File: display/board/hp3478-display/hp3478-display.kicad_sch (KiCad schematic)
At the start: 55 parts, among them J1 SFV10R-1ST, J2 DNP, U1 FT60F1x2, U2 SM16206

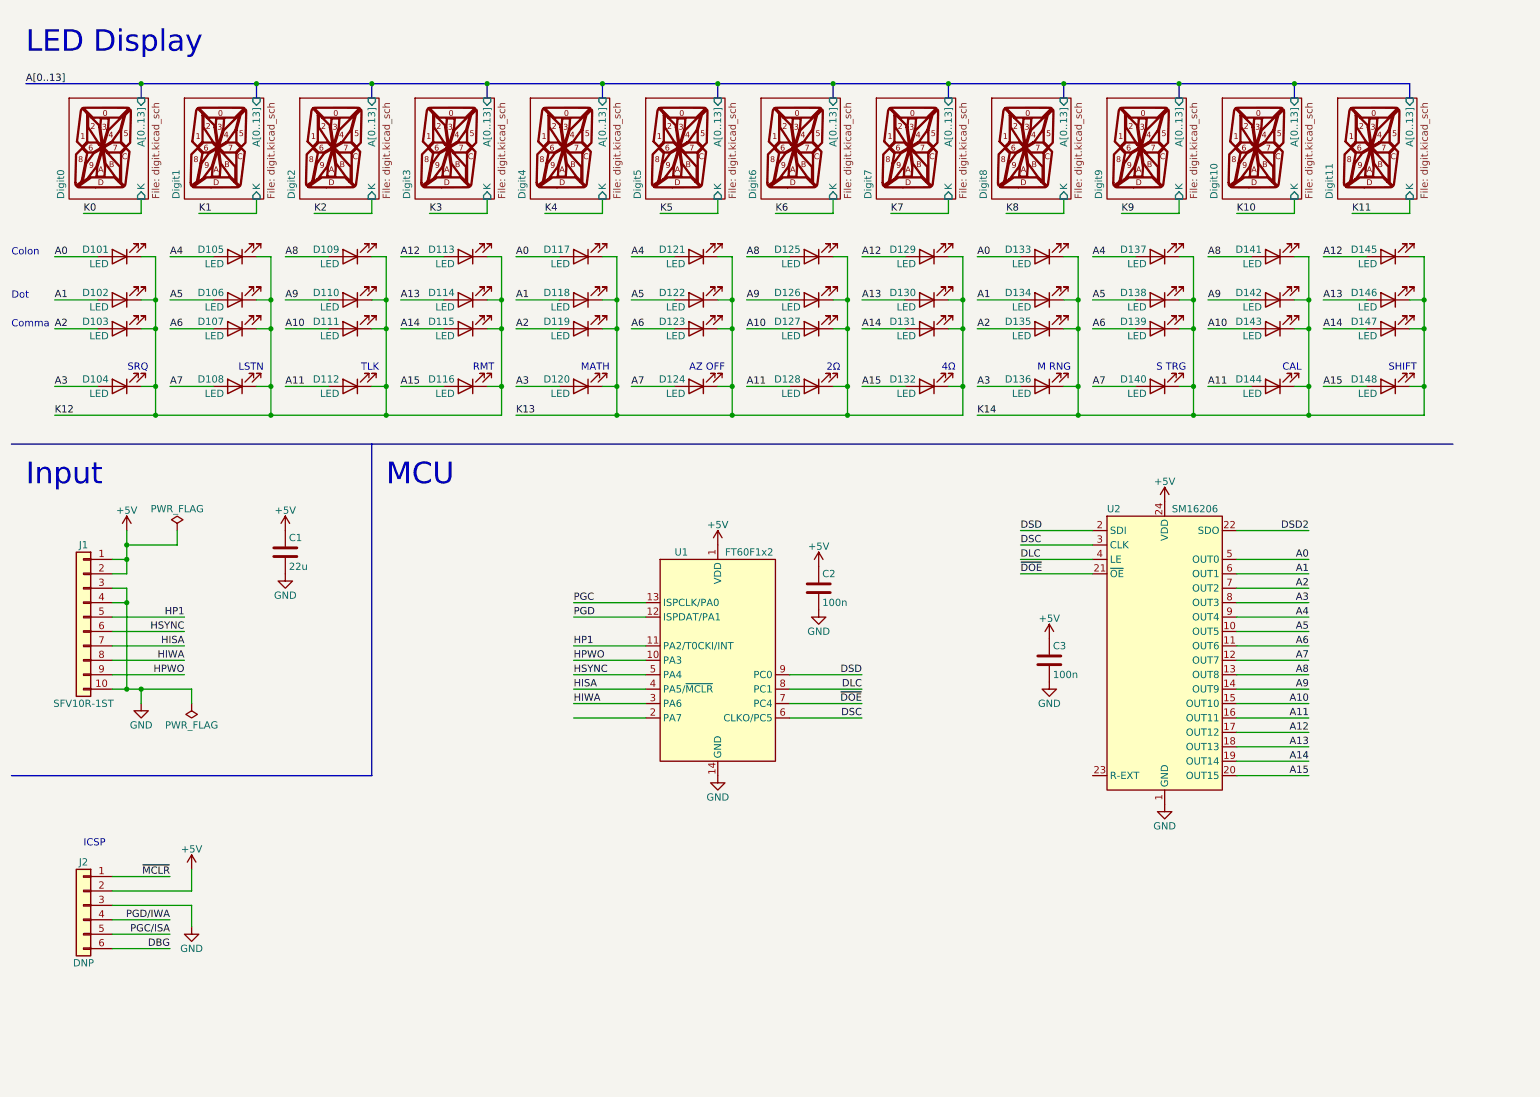
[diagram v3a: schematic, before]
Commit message: Improve workflow for getting digit shapes into KiCAD.
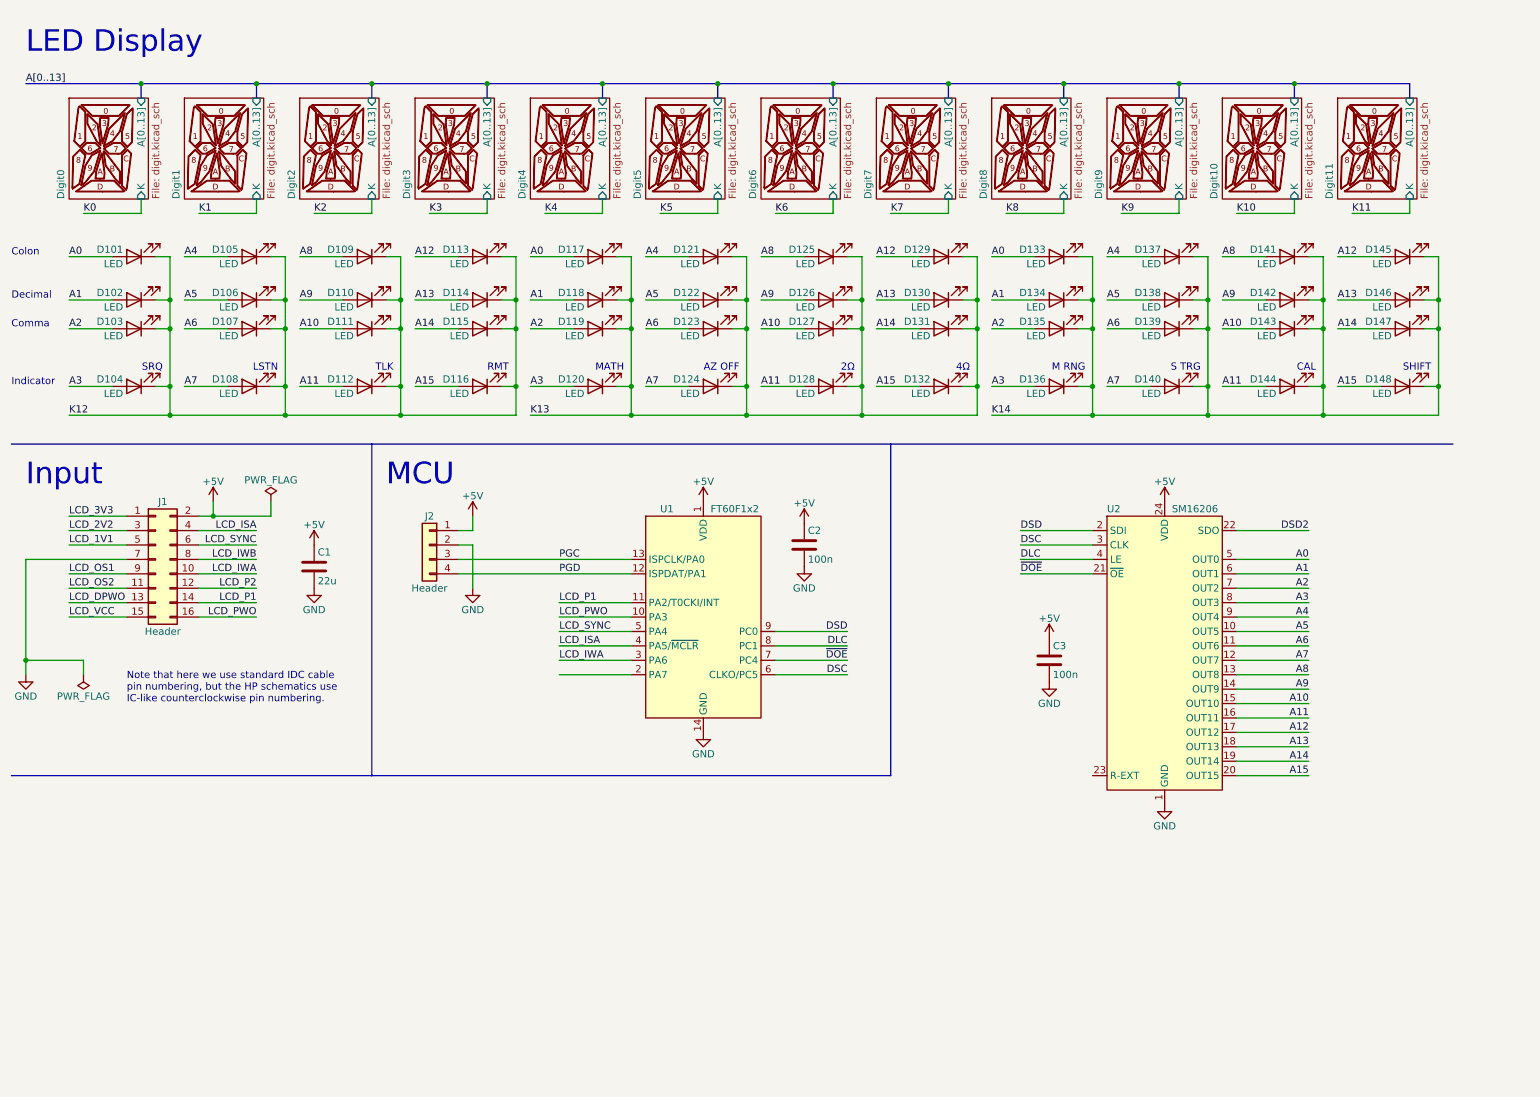
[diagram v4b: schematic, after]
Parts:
- removed J1: SFV10R-1ST, 0Local:Amphenol_SFV10R-1ST, symbol Connector_Generic:Conn_01x10
- removed J2: DNP, Connector_PinHeader_2.54mm:PinHeader_1x06_P2.54mm_Vertical, symbol Connector_Generic:Conn_01x06
- added J1: Header, Connector_PinHeader_2.54mm:PinHeader_2x08_P2.54mm_Vertical_SMD, symbol Connector_Generic:Conn_02x08_Odd_Even
- added J2: Header, Connector_PinHeader_2.54mm:PinHeader_1x04_P2.54mm_Vertical_SMD_Pin1Left, symbol Connector_Generic:Conn_01x04
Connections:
- net +5V: now also J1.2 (Pin_2), J2.1 (Pin_1)
- net GND: now also J1.7 (Pin_7), J2.2 (Pin_2)
- net PGC: now also J2.3 (Pin_3)
- net PGD: now also J2.4 (Pin_4)
- net HISA renamed LCD_ISA
- net LCD_ISA: now also J1.4 (Pin_4)
- net HIWA renamed LCD_IWA
- net LCD_IWA: now also J1.10 (Pin_10)
- net HP1 renamed LCD_P1
- net LCD_P1: now also J1.14 (Pin_14)
- net HPWO renamed LCD_PWO
- net LCD_PWO: now also J1.16 (Pin_16)
- net HSYNC renamed LCD_SYNC
- net LCD_SYNC: now also J1.6 (Pin_6)
- new net LCD_1V1: J1.5 (Pin_5)
- new net LCD_2V2: J1.3 (Pin_3)
- new net LCD_3V3: J1.1 (Pin_1)
- new net LCD_DPWO: J1.13 (Pin_13)
- new net LCD_IWB: J1.8 (Pin_8)
- new net LCD_OS1: J1.9 (Pin_9)
- new net LCD_OS2: J1.11 (Pin_11)
- new net LCD_P2: J1.12 (Pin_12)
- new net LCD_VCC: J1.15 (Pin_15)
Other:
- note added: "Decimal"
- note added: "Indicator"
- note added: "Note that here we use standard IDC cable pin numbering, but the HP schematics use IC-like counterclockwise pin numbering."
- note removed: "Dot"
- note removed: "ICSP"
- moved on the sheet: C1, C2, D101, D102, D103, D104, D105, D106, D107, D108, D109, D110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

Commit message: Add cathode drivers.
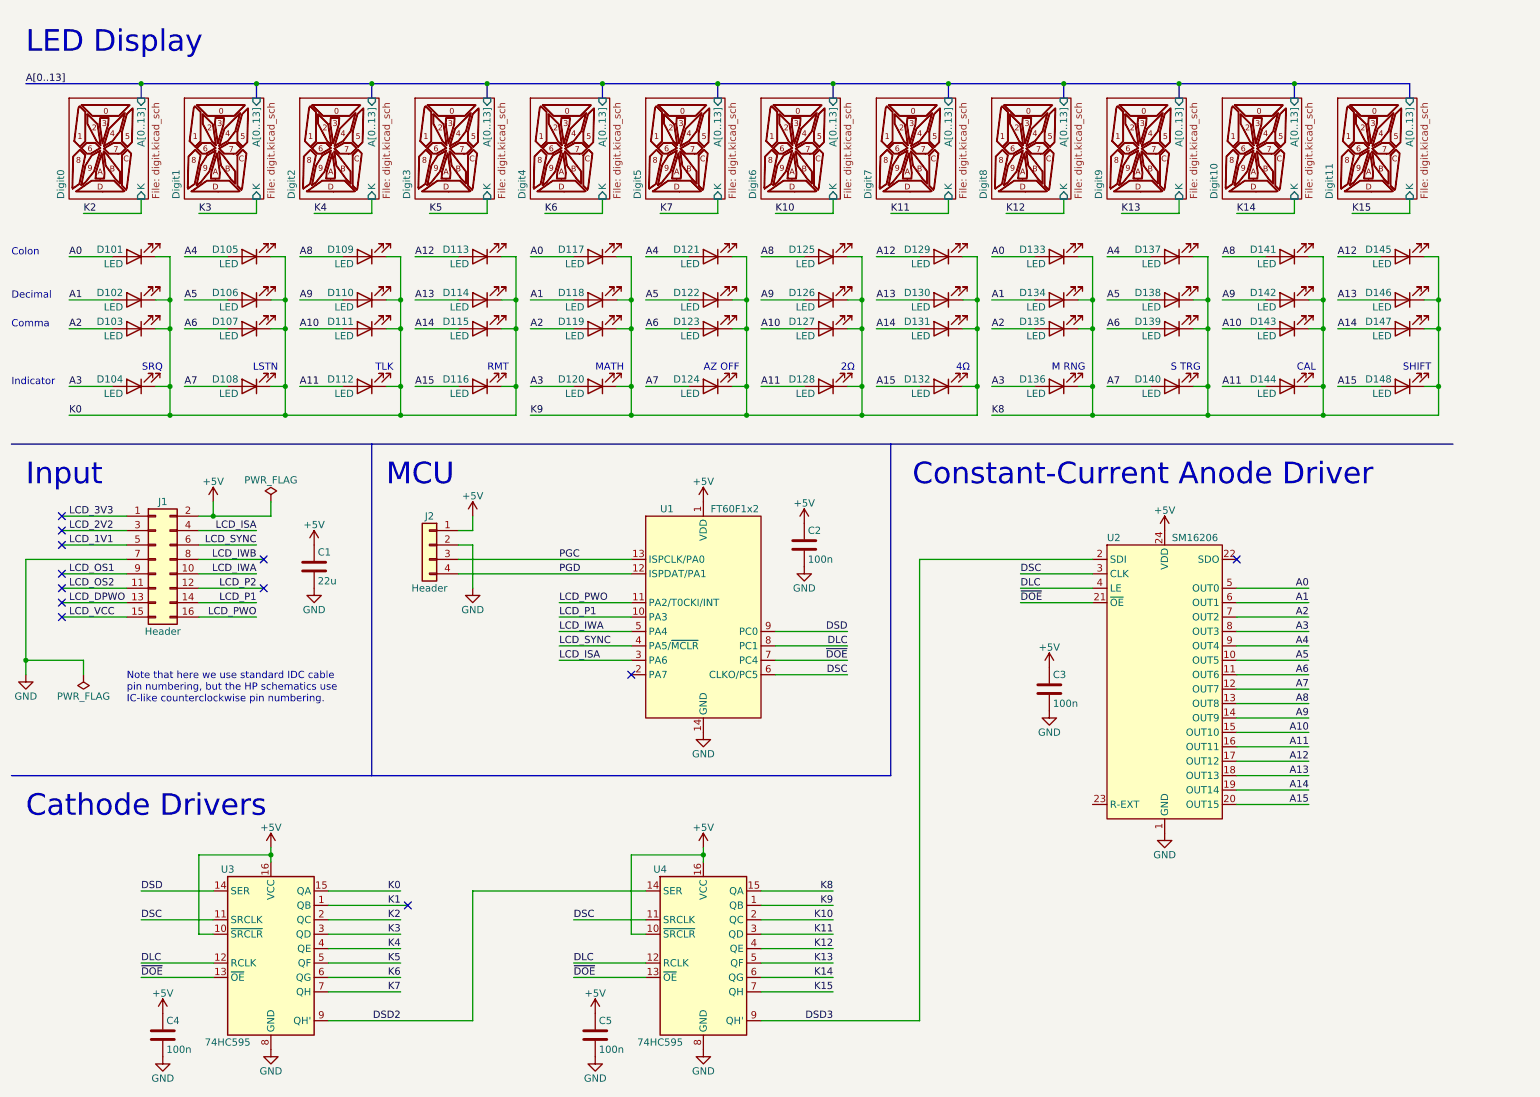
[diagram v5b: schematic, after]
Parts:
- added C4, C5: 100n, Capacitor_SMD:C_0603_1608Metric, symbol Device:C
- added U3, U4: 74HC595, Package_SO:SOIC-16_3.9x9.9mm_P1.27mm, symbol 74xx:74HC595
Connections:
- net +5V: now also C4.1, C5.1, U3.10 (~{SRCLR}), U3.16 (VCC), U4.10 (~{SRCLR}), U4.16 (VCC)
- net DLC: now also U3.12 (RCLK), U4.12 (RCLK)
- net DSC: now also U3.11 (SRCLK), U4.11 (SRCLK)
- net DSD: now also U3.14 (SER); no longer U2.2 (SDI)
- net DSD2: now also U3.9 (QH'), U4.14 (SER); no longer U2.22 (SDO)
- net GND: now also C4.2, C5.2, U3.8 (GND), U4.8 (GND)
- net K0: now also D101.1 (K), D102.1 (K), D103.1 (K), D104.1 (K), D105.1 (K), D106.1 (K), D107.1 (K), D108.1 (K), D109.1 (K), D110.1 (K), D111.1 (K), D112.1 (K), D113.1 (K), D114.1 (K), D115.1 (K), D116.1 (K), U3.15 (QA)
- net K1: now also U3.1 (QB)
- net K10: now also U4.2 (QC)
- net K11: now also U4.3 (QD)
- net K12: now also U4.4 (QE); no longer D101.1 (K), D102.1 (K), D103.1 (K), D104.1 (K), D105.1 (K), D106.1 (K), D107.1 (K), D108.1 (K), D109.1 (K), D110.1 (K), D111.1 (K), D112.1 (K), D113.1 (K), D114.1 (K), D115.1 (K), D116.1 (K)
- net K13: now also U4.5 (QF); no longer D117.1 (K), D118.1 (K), D119.1 (K), D120.1 (K), D121.1 (K), D122.1 (K), D123.1 (K), D124.1 (K), D125.1 (K), D126.1 (K), D127.1 (K), D128.1 (K), D129.1 (K), D130.1 (K), D131.1 (K), D132.1 (K)
- net K14: now also U4.6 (QG); no longer D133.1 (K), D134.1 (K), D135.1 (K), D136.1 (K), D137.1 (K), D138.1 (K), D139.1 (K), D140.1 (K), D141.1 (K), D142.1 (K), D143.1 (K), D144.1 (K), D145.1 (K), D146.1 (K), D147.1 (K), D148.1 (K)
- net K2: now also U3.2 (QC)
- net K3: now also U3.3 (QD)
- net K4: now also U3.4 (QE)
- net K5: now also U3.5 (QF)
- net K6: now also U3.6 (QG)
- net K7: now also U3.7 (QH)
- net K8: now also D133.1 (K), D134.1 (K), D135.1 (K), D136.1 (K), D137.1 (K), D138.1 (K), D139.1 (K), D140.1 (K), D141.1 (K), D142.1 (K), D143.1 (K), D144.1 (K), D145.1 (K), D146.1 (K), D147.1 (K), D148.1 (K), U4.15 (QA)
- net K9: now also D117.1 (K), D118.1 (K), D119.1 (K), D120.1 (K), D121.1 (K), D122.1 (K), D123.1 (K), D124.1 (K), D125.1 (K), D126.1 (K), D127.1 (K), D128.1 (K), D129.1 (K), D130.1 (K), D131.1 (K), D132.1 (K), U4.1 (QB)
- net LCD_ISA: now also U1.3 (PA6); no longer U1.4 (PA5/~{MCLR})
- net LCD_IWA: now also U1.5 (PA4); no longer U1.3 (PA6)
- net LCD_P1: now also U1.10 (PA3); no longer U1.11 (PA2/T0CKI/INT)
- net LCD_PWO: now also U1.11 (PA2/T0CKI/INT); no longer U1.10 (PA3)
- net LCD_SYNC: now also U1.4 (PA5/~{MCLR}); no longer U1.5 (PA4)
- net ~{DOE}: now also U3.13 (~{OE}), U4.13 (~{OE})
- new net DSD3: U2.2 (SDI), U4.9 (QH')
- new net K15: U4.7 (QH)
- no-connect marks 0 -> 12
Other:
- note added: "Cathode Drivers"
- note added: "Constant-Current Anode Driver"
- moved on the sheet: C3, U2

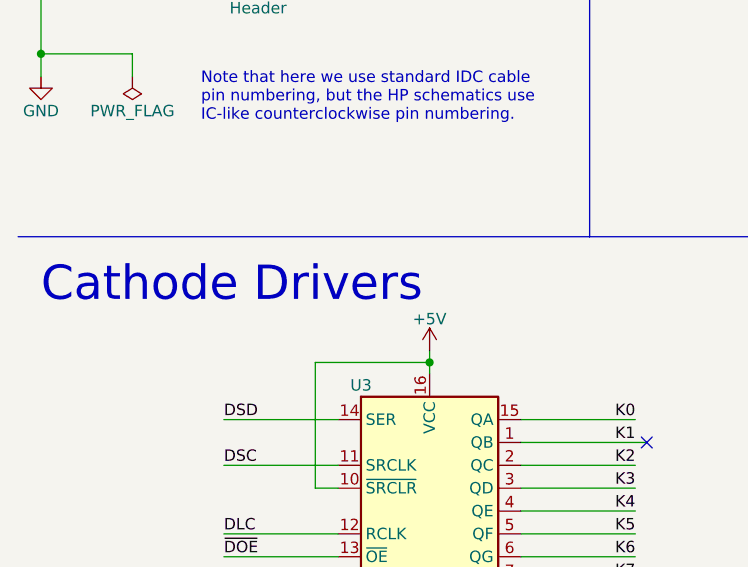
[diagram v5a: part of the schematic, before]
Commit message: Move silkscreen clear of vias.
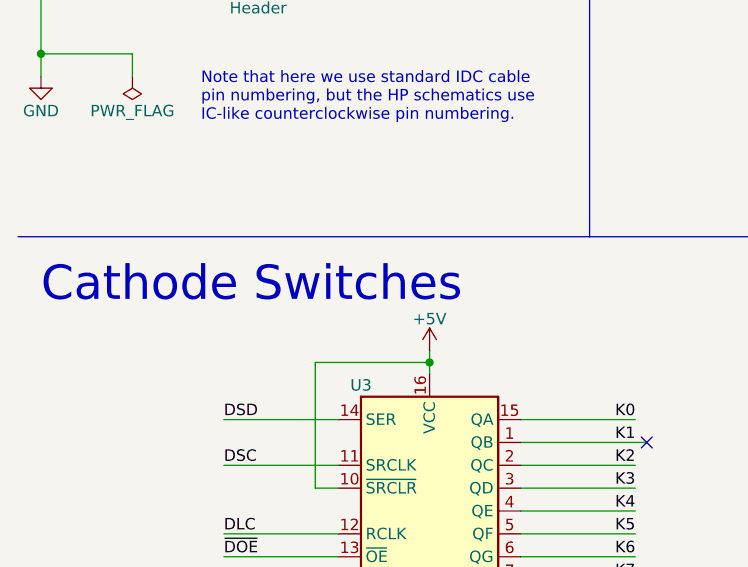
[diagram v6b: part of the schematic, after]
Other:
- note added: "Cathode Switches"
- note removed: "Cathode Drivers"
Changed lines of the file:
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@@
     (effects (font (size 3.81 3.81)) (justify left bottom))
   )
-  (text "Cathode Drivers" (at 15.24 154.94 0)
+  (text "Cathode Switches" (at 15.24 154.94 0)
     (effects (font (size 3.81 3.81)) (justify left bottom))
   )
